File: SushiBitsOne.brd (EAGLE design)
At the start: 68.6 x 53.3 mm, 68 parts, among them IC1 STM32F042F6P6, IC2 LM3671-3.3DBV, IC3 TPS562200DBV, J1 ARDUINO_R3, J2 DC-005, Q1 2N7002, Q2 MMBT2222A, U1 STM32F103CBT6-LQFP48, X1 32768Hz, X2 8MHz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

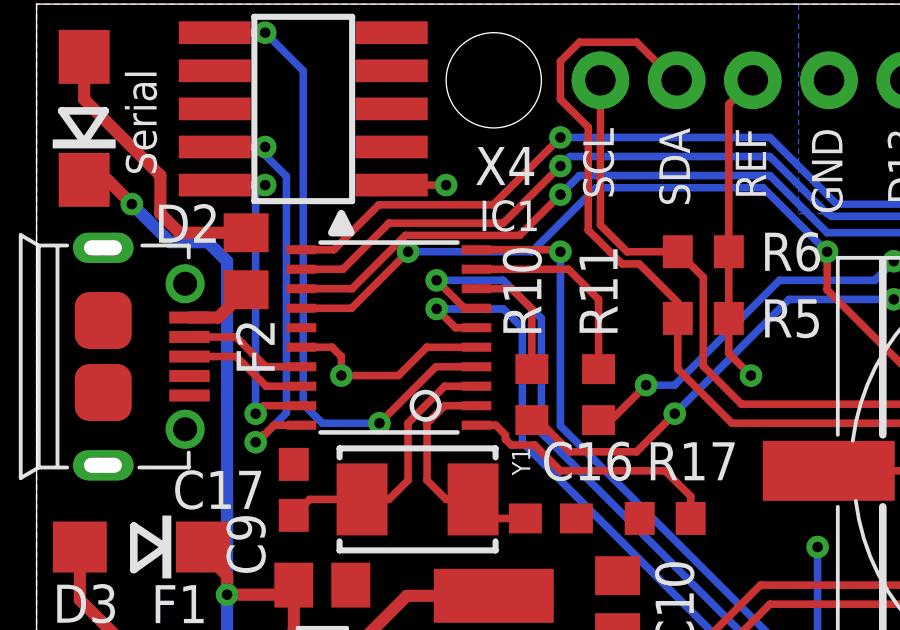
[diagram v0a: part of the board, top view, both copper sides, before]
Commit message: There is a net overlap.
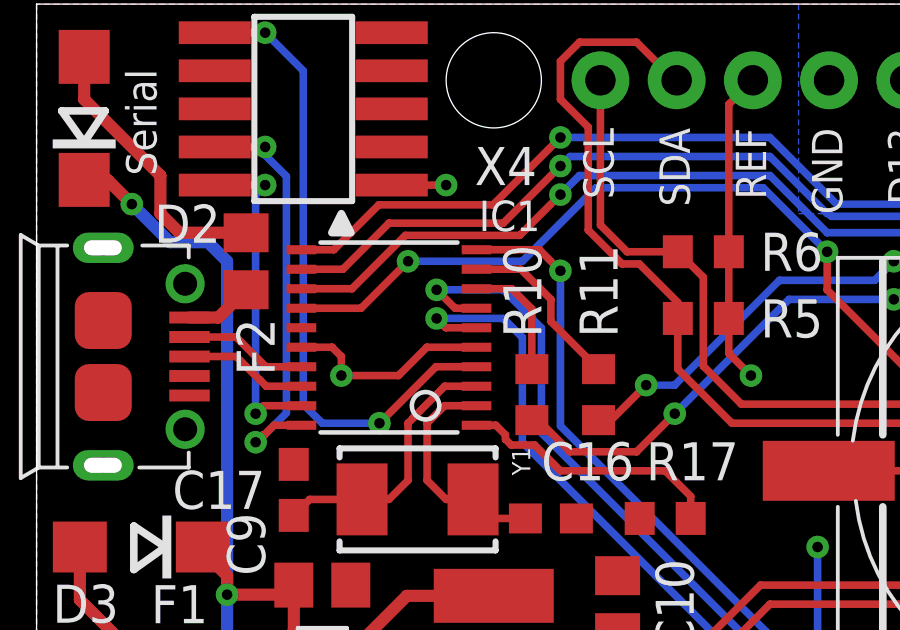
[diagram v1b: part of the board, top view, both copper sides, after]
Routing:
- net N$22: track 6.81 -> 5.88 mm
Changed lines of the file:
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@@
 <wire x1="65.17749375" y1="23.8125" x2="63.64000625" y2="25.3499875" width="0.254" layer="1"/>
 <contactref element="IC1" pad="10"/>
-<wire x1="14.6653" y1="45.1525" x2="17.2125" y2="45.1525" width="0.254" layer="1"/>
-<wire x1="17.2125" y1="45.1525" x2="17.4625" y2="45.085" width="0.254" layer="1"/>
-<via x="17.4625" y="45.085" extent="1-16" drill="0.35"/>
 <wire x1="24.3284" y1="32.41270625" x2="24.3284" y2="29.9641" width="0.254" layer="16"/>
 <wire x1="24.3284" y1="29.9641" x2="35.8775" y2="18.415" width="0.254" layer="16"/>
-<wire x1="17.4625" y1="45.085" x2="17.4625" y2="39.27860625" width="0.254" layer="16"/>
 <wire x1="17.4625" y1="39.27860625" x2="24.3284" y2="32.41270625" width="0.254" layer="16"/>
 <via x="35.8775" y="18.415" extent="1-16" drill="0.35"/>
+<wire x1="14.6653" y1="45.1525" x2="16.76" y2="45.1525" width="0.254" layer="1"/>
+<wire x1="16.76" y1="45.1525" x2="17.4625" y2="44.45" width="0.254" layer="1"/>
+<via x="17.4625" y="44.45" extent="1-16" drill="0.35"/>
+<wire x1="17.4625" y1="44.45" x2="17.4625" y2="39.27860625" width="0.254" layer="16"/>
 </signal>
 <signal name="D14">
@@
 <contactref element="IC1" pad="9"/>
 <contactref element="R11" pad="1"/>
-<wire x1="14.6653" y1="44.5025" x2="17.7275" y2="44.5025" width="0.254" layer="1"/>
-<wire x1="17.7275" y1="44.5025" x2="18.7325" y2="43.4975" width="0.254" layer="1"/>
-<wire x1="18.7325" y1="43.4975" x2="18.7325" y2="41.1725" width="0.254" layer="1"/>
+<wire x1="14.6653" y1="44.5025" x2="16.14" y2="44.5025" width="0.254" layer="1"/>
+<wire x1="16.14" y1="44.5025" x2="17.145" y2="43.4975" width="0.254" layer="1"/>
+<wire x1="17.145" y1="43.4975" x2="17.145" y2="42.76" width="0.254" layer="1"/>
+<wire x1="17.145" y1="42.76" x2="18.7325" y2="41.1725" width="0.254" layer="1"/>
 </signal>
 <signal name="N$23">
@@
 <contactref element="IC1" pad="14"/>
 <contactref element="RN1" pad="4"/>
-<wire x1="8.8297" y1="43.2025" x2="10.5" y2="43.2025" width="0.254" layer="1"/>
-<wire x1="10.5" y1="43.2025" x2="12.3825" y2="45.085" width="0.254" layer="1"/>
-<via x="12.3825" y="45.085" extent="1-16" drill="0.35"/>
-<wire x1="12.3825" y1="45.085" x2="16.51" y2="45.085" width="0.254" layer="16"/>
-<wire x1="16.51" y1="45.085" x2="18.6436" y2="47.2186" width="0.254" layer="16"/>
+<wire x1="8.8297" y1="43.2025" x2="10.8175" y2="43.2025" width="0.254" layer="1"/>
+<wire x1="10.8175" y1="43.2025" x2="12.3825" y2="44.7675" width="0.254" layer="1"/>
+<via x="12.3825" y="44.7675" extent="1-16" drill="0.35"/>
+<wire x1="12.3825" y1="44.7675" x2="16.1925" y2="44.7675" width="0.254" layer="16"/>
+<wire x1="16.1925" y1="44.7675" x2="18.6436" y2="47.2186" width="0.254" layer="16"/>
 <wire x1="18.6436" y1="47.2186" x2="24.2189" y2="47.2186" width="0.254" layer="16"/>
 <wire x1="24.2189" y1="47.2186" x2="26.3525" y2="45.085" width="0.254" layer="16"/>
@@
 <contactref element="IC1" pad="6"/>
 <contactref element="LED3" pad="C"/>
-<wire x1="14.6653" y1="42.5525" x2="13.9625" y2="42.5525" width="0.254" layer="1"/>
-<wire x1="13.9625" y1="42.5525" x2="13.335" y2="43.18" width="0.254" layer="1"/>
-<via x="13.335" y="43.18" extent="1-16" drill="0.35"/>
-<wire x1="13.335" y1="43.18" x2="15.5575" y2="43.18" width="0.254" layer="16"/>
-<wire x1="15.5575" y1="43.18" x2="16.1925" y2="42.545" width="0.254" layer="16"/>
-<wire x1="16.1925" y1="42.545" x2="16.1925" y2="38.735" width="0.254" layer="16"/>
+<wire x1="14.6653" y1="42.5525" x2="13.645" y2="42.5525" width="0.254" layer="1"/>
+<wire x1="13.645" y1="42.5525" x2="13.335" y2="42.8625" width="0.254" layer="1"/>
+<via x="13.335" y="42.8625" extent="1-16" drill="0.35"/>
+<wire x1="13.335" y1="42.8625" x2="15.5575" y2="42.8625" width="0.254" layer="16"/>
+<wire x1="15.5575" y1="42.8625" x2="16.1925" y2="42.2275" width="0.254" layer="16"/>
+<wire x1="16.1925" y1="42.2275" x2="16.1925" y2="38.735" width="0.254" layer="16"/>
 <wire x1="16.1925" y1="38.735" x2="23.1775" y2="31.75" width="0.254" layer="16"/>
 <wire x1="23.1775" y1="31.75" x2="23.1775" y2="30.4574875" width="0.254" layer="16"/>
@@
 <contactref element="IC1" pad="7"/>
 <contactref element="LED4" pad="C"/>
-<wire x1="14.6653" y1="43.2025" x2="14.265" y2="43.2025" width="0.254" layer="1"/>
-<wire x1="14.265" y1="43.2025" x2="13.335" y2="44.1325" width="0.254" layer="1"/>
-<via x="13.335" y="44.1325" extent="1-16" drill="0.35"/>
-<wire x1="13.335" y1="44.1325" x2="15.5575" y2="44.1325" width="0.254" layer="16"/>
-<wire x1="15.5575" y1="44.1325" x2="16.8275" y2="42.8625" width="0.254" layer="16"/>
-<wire x1="16.8275" y1="42.8625" x2="16.8275" y2="39.0525" width="0.254" layer="16"/>
+<wire x1="14.6653" y1="43.2025" x2="13.9475" y2="43.2025" width="0.254" layer="1"/>
+<wire x1="13.9475" y1="43.2025" x2="13.335" y2="43.815" width="0.254" layer="1"/>
+<via x="13.335" y="43.815" extent="1-16" drill="0.35"/>
+<wire x1="13.335" y1="43.815" x2="15.5575" y2="43.815" width="0.254" layer="16"/>
+<wire x1="15.5575" y1="43.815" x2="16.8275" y2="42.545" width="0.254" layer="16"/>
+<wire x1="16.8275" y1="42.545" x2="16.8275" y2="39.0525" width="0.254" layer="16"/>
 <wire x1="16.8275" y1="39.0525" x2="23.8125" y2="32.0675" width="0.254" layer="16"/>
 <wire x1="23.8125" y1="32.0675" x2="23.8125" y2="29.5275" width="0.254" layer="16"/>
@@
 </signal>
 </signals>
+<errors>
+</errors>
 </board>
 </drawing>
